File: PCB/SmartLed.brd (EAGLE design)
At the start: 82.5 x 70 mm, 46 parts, among them IC2 DS1307, IC3 MEGA8-P, K1 G5LE, Q1 32.768khz, T1 BC337

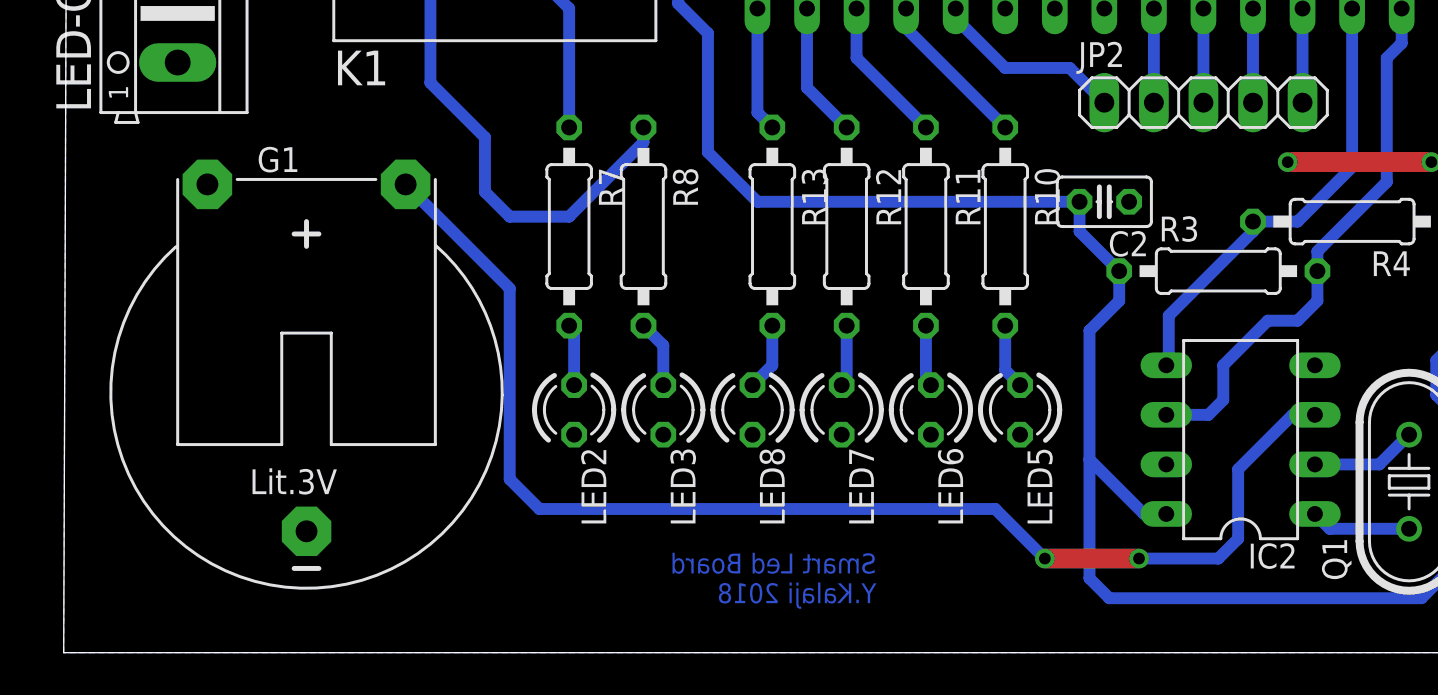
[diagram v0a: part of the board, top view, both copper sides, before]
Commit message: Add 100n capacitor beside 3.6v lithium battery & change the battery footprint
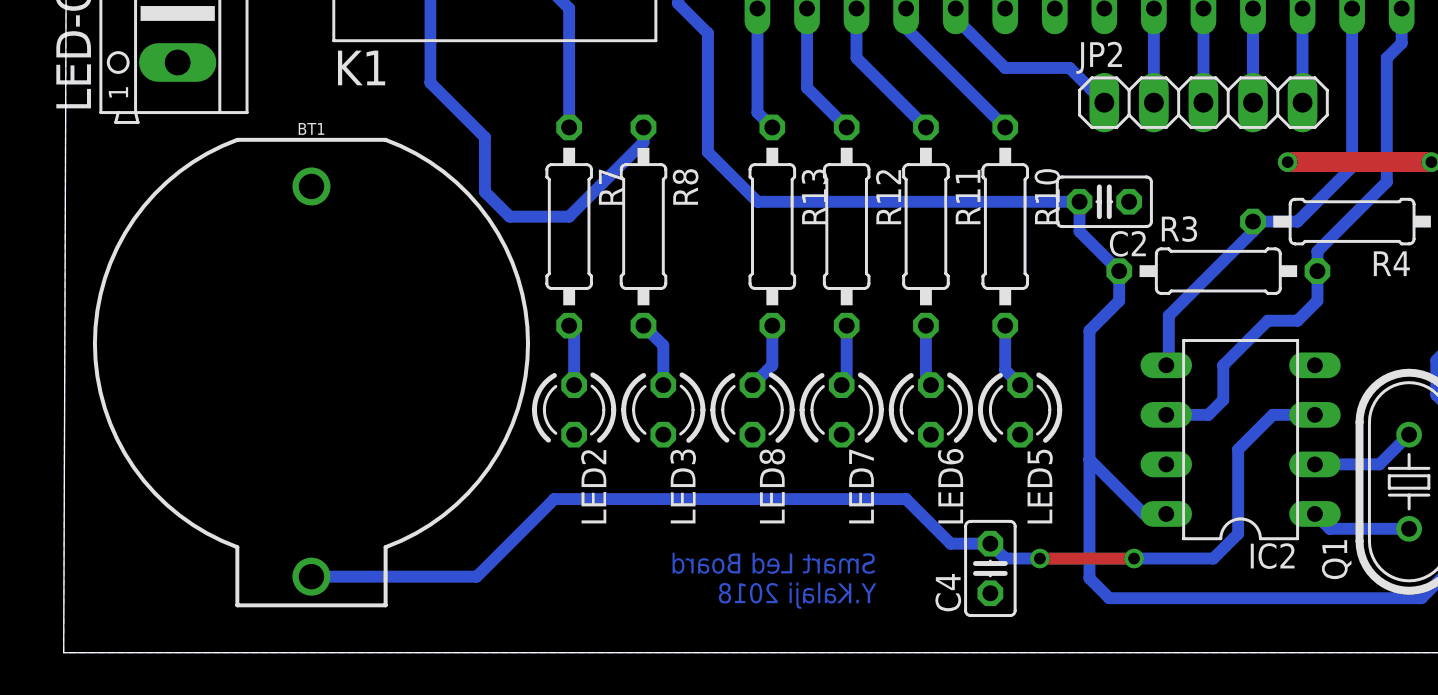
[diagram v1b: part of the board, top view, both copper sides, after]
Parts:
- removed G1: CR2032H, battery:CR2032H
- added BT1: (no value), SparkFun-Batteries:BATTCOM_20MM_PTH
- added C4: 100nf, rcl:C025-025X050
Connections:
- removed net N$18: G1.+, IC2.3
- new net N$44: BT1.1, C4.2, IC2.3
- net GND: now also BT1.2, C4.1; no longer G1.-
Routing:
- net N$18: track 65.4 -> 0.00 mm, vias 2 -> 0
- net N$44: track 0.00 -> 59.9 mm, vias 0 -> 2
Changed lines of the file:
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@@
 <layer number="112" name="tSilk" color="7" fill="1" visible="no" active="yes"/>
 <layer number="113" name="ReferenceLS" color="7" fill="1" visible="no" active="no"/>
+<layer number="114" name="Badge_Outline" color="7" fill="1" visible="yes" active="yes"/>
+<layer number="115" name="ReferenceISLANDS" color="7" fill="1" visible="yes" active="yes"/>
 <layer number="116" name="Patch_BOT" color="9" fill="4" visible="no" active="yes"/>
 <layer number="118" name="Rect_Pads" color="7" fill="1" visible="no" active="no"/>
@@
 <element name="C3" library="rcl" package="E2,5-5" value="4.7uf" x="56.642" y="88.9" rot="R270"/>
 <element name="D1" library="diode" package="DO35-7" value="1N4148DO35-7" x="22.098" y="86.36"/>
-<element name="G1" library="battery" package="CR2032H" value="CR2032H" x="8.636" y="42.926"/>
 <element name="IC2" library="adafruit" package="DIL08" value="DS1307" x="56.515" y="40.64" rot="R90"/>
 <element name="IC3" library="atmel" package="DIL28-3" value="MEGA8-P" x="48.26" y="66.548" rot="R180">
@@
 <element name="JP2" library="pinhead" package="1X05" value="" x="54.61" y="57.912"/>
 <element name="C1" library="rcl" package="E2,5-5" value="4.7uf" x="73.406" y="34.798" rot="R270"/>
+<element name="C4" library="rcl" package="C025-025X050" value="100nf" x="43.688" y="34.036" rot="R90"/>
+<element name="BT1" library="SparkFun-Batteries" package="BATTCOM_20MM_PTH" value="" x="8.89" y="45.466" rot="R270">
+<attribute name="SF_SKU" value="PRT-00783" x="8.89" y="45.466" size="1.778" layer="27" rot="R270" display="off"/>
+<attribute name="PROD_ID" value="BATT-09031" x="8.89" y="45.466" size="1.778" layer="27" rot="R270" display="off"/>
+</element>
 </elements>
 <signals>
@@
 <contactref element="OK1" pad="3"/>
 <contactref element="IC2" pad="4"/>
-<contactref element="G1" pad="-"/>
 <contactref element="IC3" pad="8"/>
 <contactref element="T1" pad="1"/>
@@
 <via x="73.152" y="58.42" extent="1-16" drill="0.6" shape="square"/>
 <contactref element="C1" pad="-"/>
+<contactref element="C4" pad="1"/>
+<contactref element="BT1" pad="2"/>
 </signal>
 <signal name="AVCC">
@@
 <wire x1="59.436" y1="51.816" x2="62.23" y2="54.61" width="0.6096" layer="16"/>
 </signal>
-<signal name="N$18">
-<contactref element="G1" pad="+"/>
-<contactref element="IC2" pad="3"/>
-<wire x1="43.942" y1="37.084" x2="20.574" y2="37.084" width="0.6096" layer="16"/>
-<wire x1="20.574" y1="37.084" x2="19.05" y2="38.608" width="0.6096" layer="16"/>
-<wire x1="19.05" y1="38.608" x2="19.05" y2="48.387" width="0.6096" layer="16"/>
-<wire x1="19.05" y1="48.387" x2="13.716" y2="53.721" width="0.6096" layer="16"/>
-<wire x1="60.325" y1="41.91" x2="59.182" y2="41.91" width="0.6096" layer="16"/>
-<wire x1="59.182" y1="41.91" x2="56.388" y2="39.116" width="0.6096" layer="16"/>
-<wire x1="56.388" y1="39.116" x2="56.388" y2="35.56" width="0.6096" layer="16"/>
-<wire x1="56.388" y1="35.56" x2="55.372" y2="34.544" width="0.6096" layer="16"/>
-<wire x1="55.372" y1="34.544" x2="51.308" y2="34.544" width="0.6096" layer="16"/>
-<via x="51.308" y="34.544" extent="1-16" drill="0.6" shape="square"/>
-<wire x1="51.308" y1="34.544" x2="46.482" y2="34.544" width="1.016" layer="1"/>
-<via x="46.482" y="34.544" extent="1-16" drill="0.6" shape="square"/>
-<wire x1="43.942" y1="37.084" x2="46.482" y2="34.544" width="0.6096" layer="16"/>
-</signal>
 <signal name="N$21">
 <contactref element="Q1" pad="1"/>
@@
 <wire x1="47.752" y1="59.69" x2="44.45" y2="59.69" width="0.6096" layer="16"/>
 </signal>
+<signal name="N$44">
+<contactref element="C4" pad="2"/>
+<contactref element="IC2" pad="3"/>
+<contactref element="BT1" pad="1"/>
+<wire x1="8.89" y1="33.616" x2="17.36" y2="33.616" width="0.6096" layer="16"/>
+<wire x1="17.36" y1="33.616" x2="21.336" y2="37.592" width="0.6096" layer="16"/>
+<wire x1="21.336" y1="37.592" x2="39.37" y2="37.592" width="0.6096" layer="16"/>
+<wire x1="39.37" y1="37.592" x2="41.656" y2="35.306" width="0.6096" layer="16"/>
+<wire x1="41.656" y1="35.306" x2="43.688" y2="35.306" width="0.6096" layer="16"/>
+<via x="46.228" y="34.544" extent="1-16" drill="0.6" shape="square"/>
+<wire x1="46.228" y1="34.544" x2="51.054" y2="34.544" width="0.6096" layer="1"/>
+<via x="51.054" y="34.544" extent="1-16" drill="0.6" shape="square"/>
+<wire x1="51.054" y1="34.544" x2="55.118" y2="34.544" width="0.6096" layer="16"/>
+<wire x1="55.118" y1="34.544" x2="56.388" y2="35.814" width="0.6096" layer="16"/>
+<wire x1="56.388" y1="35.814" x2="56.388" y2="40.132" width="0.6096" layer="16"/>
+<wire x1="56.388" y1="40.132" x2="58.166" y2="41.91" width="0.6096" layer="16"/>
+<wire x1="58.166" y1="41.91" x2="60.325" y2="41.91" width="0.6096" layer="16"/>
+<wire x1="43.688" y1="35.306" x2="44.45" y2="34.544" width="0.6096" layer="16"/>
+<wire x1="44.45" y1="34.544" x2="46.228" y2="34.544" width="0.6096" layer="16"/>
+</signal>
 </signals>

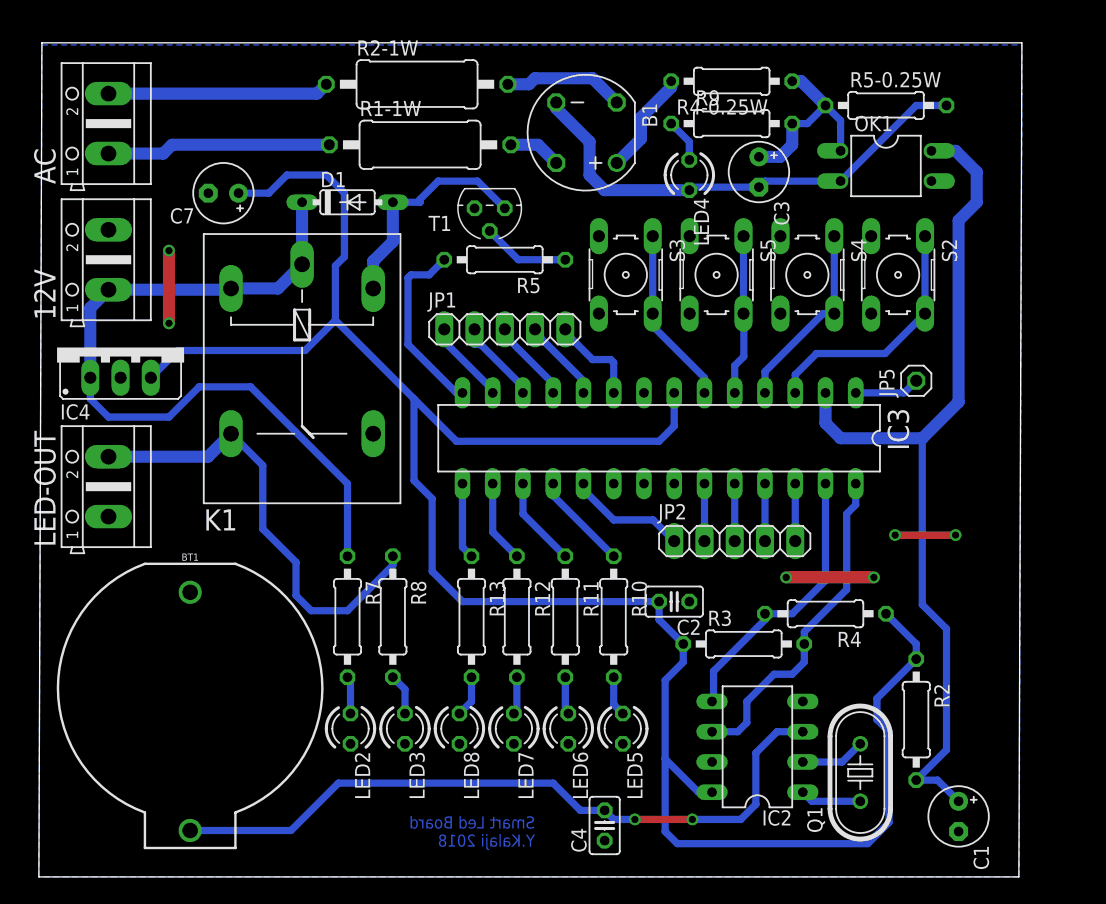
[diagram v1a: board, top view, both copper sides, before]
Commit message: Infrared receiver was added & crystal footprint size was corrected
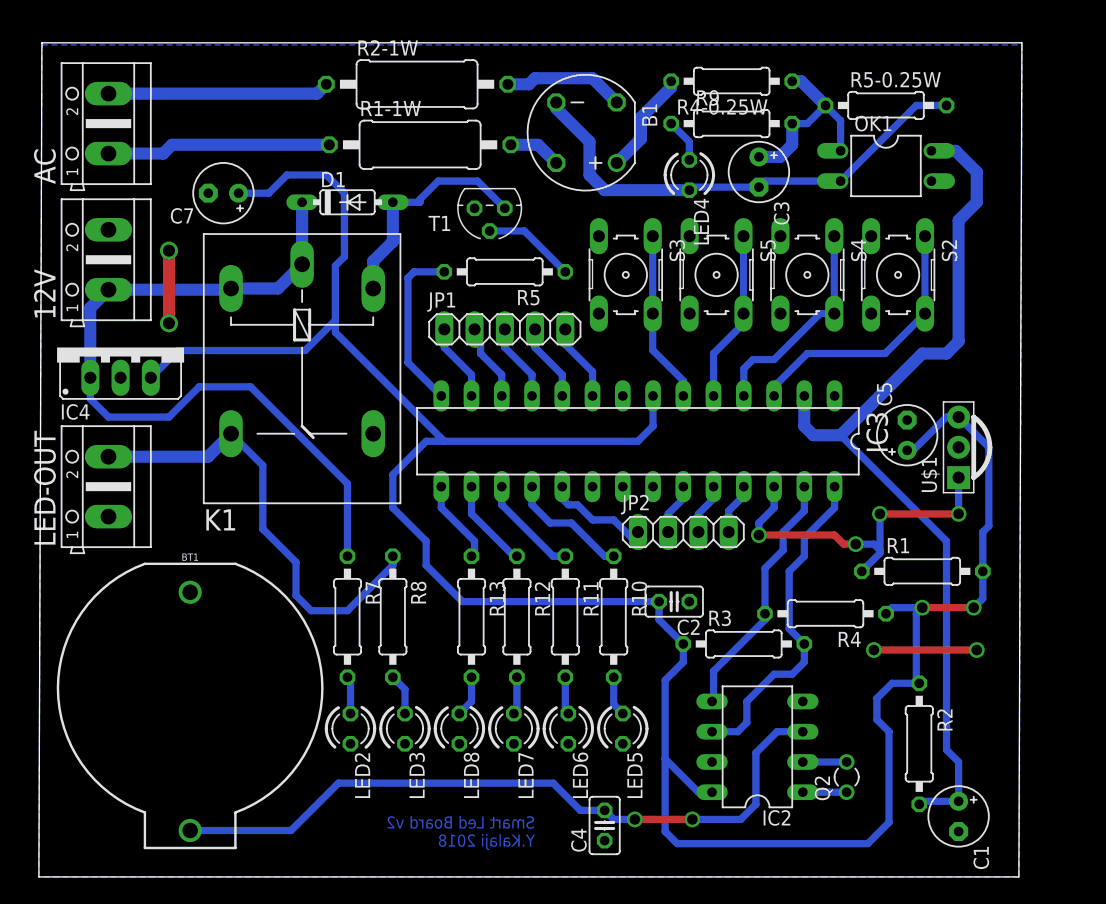
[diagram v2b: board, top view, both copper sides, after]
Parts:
- removed JP5: (no value), pinhead:1X01
- removed Q1: 32.768khz, crystal:HC49U70
- added C5: 4.7uf, rcl:E2,5-5
- added Q2: 32.768khz, crystal:TC26V
- added R1: 10k, rcl:0207/10
- added U$1: PNA460XM, adafruit:PNA460XM
- JP2: device pinhead:1X05 -> pinhead:1X04
- moved JP2 4.38 mm to (50.3, 58.7)
- moved R2 2.05 mm to (70.1, 40.9)
- moved IC3 1.80 mm to (46.5, 66.3)
- moved R5 1.02 mm to (35.3, 80.5)
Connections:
- removed net N$36: IC3.26, JP2.5
- removed net N$43: IC3.1, JP5.1
- new net N$46: IC3.26, R1.1, U$1.1
- net +5V: now also C5.+, R1.2, U$1.3
- net GND: now also C5.-, U$1.2
- net N$21: now also Q2.1; no longer Q1.1
- net N$22: now also Q2.2; no longer Q1.2
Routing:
- net N$46: track 0.00 -> 30.4 mm, vias 0 -> 4
- net +5V: track 176.0 -> 206.3 mm, vias 0 -> 2
- net N$43: track 5.50 -> 0.00 mm
- net N$36: track 4.83 -> 0.00 mm
- net GND: track 18.5 -> 14.7 mm, vias 6 -> 4
- net N$13: track 23.6 -> 21.2 mm
- net N$32: track 16.1 -> 18.3 mm
- net N$26: track 8.20 -> 10.2 mm
- net N$11: track 74.9 -> 76.7 mm
- net N$22: track 5.46 -> 3.68 mm
- net N$21: track 5.14 -> 3.68 mm
- net N$41: track 7.91 -> 6.53 mm
- net N$10: track 15.5 -> 14.3 mm
- net N$24: track 7.57 -> 8.65 mm
- net N$40: track 9.92 -> 8.94 mm
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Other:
- board text added: "Smart Led Board v2 Y.Kalaji 2018"
- board text removed: "Smart Led Board Y.Kalaji 2018"

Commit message: Refactor PCB design (several enhancements)
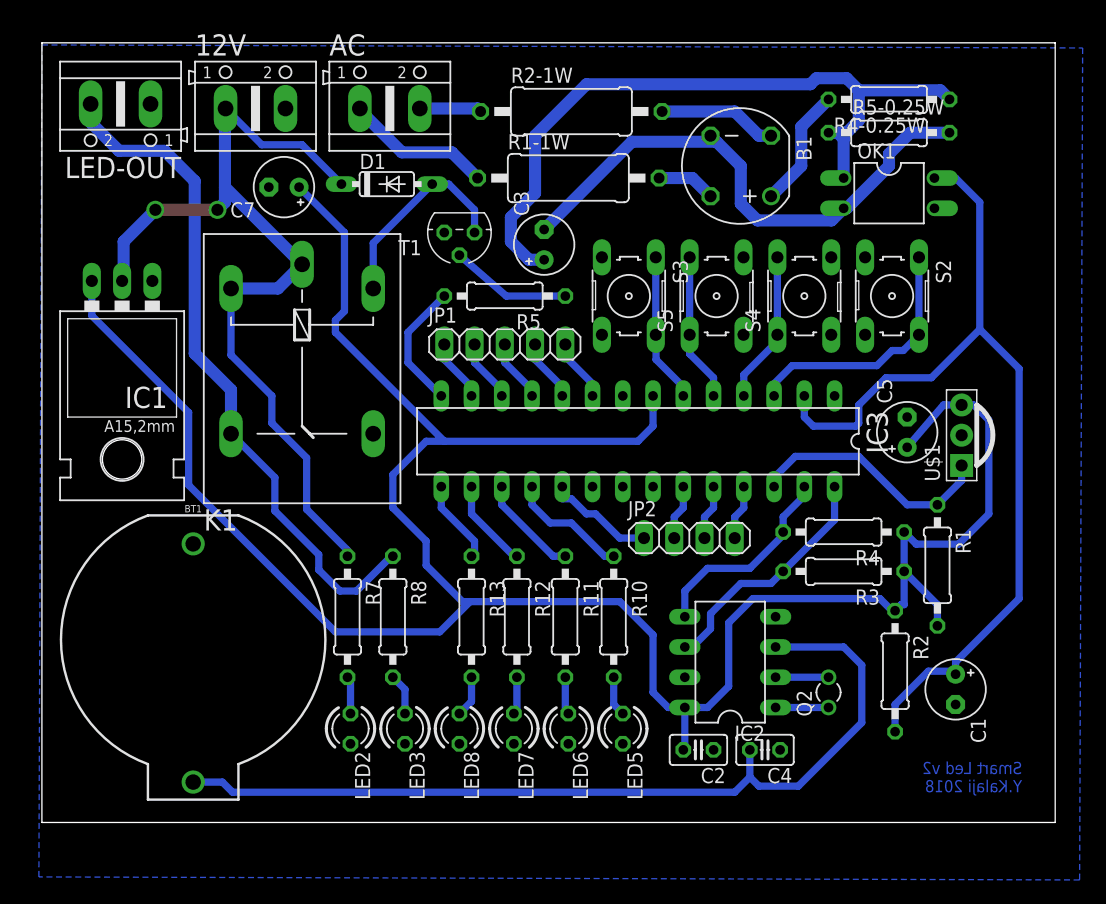
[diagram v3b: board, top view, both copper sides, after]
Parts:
- removed IC4: (no value), v-reg:78XXS
- removed LED4: (no value), led:LED3MM
- removed R9: 330, rcl:0207/10
- added IC1: (no value), v-reg:79XXL
- moved LED-OUT 32.1 mm to (3.05, 94.6), turned to 180 degrees
- moved AC 23.7 mm to (25.7, 94.2), turned to 0 degrees
- moved C3 19.0 mm to (38.6, 82.8), turned to 90 degrees
- moved 12V 17.7 mm to (14.4, 94.2), turned to 0 degrees
- moved C4 14.9 mm to (57.1, 40.4), turned to 180 degrees
- moved R4-0.25W 13.3 mm to (67.6, 95.0)
- moved B1 13.3 mm to (55.1, 89.4)
- moved R2-1W 13.2 mm to (40.9, 94.0)
- moved R1-1W 12.8 mm to (40.6, 88.4)
- moved C2 12.6 mm to (51.6, 40.4)
- moved C1 10.7 mm to (73.2, 45.5)
- moved R3 10.4 mm to (63.8, 55.4), turned to 180 degrees
- moved IC2 7.47 mm to (54.2, 47.8)
- moved Q2 7.27 mm to (62.5, 45.2)
- moved R4 7.03 mm to (63.8, 58.7)
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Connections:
- removed net N$19: LED4.A, R9.1
- net +12V: now also IC1.IN; no longer IC4.IN
- net +5V: now also IC1.OUT; no longer IC4.OUT
- net GND: now also IC1.GND; no longer IC4.GND
- net N$6: no longer R9.2
- net N$7: no longer LED4.K
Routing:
- net N$6: track 16.4 -> 60.2 mm
- net N$8: track 37.9 -> 57.5 mm
- net GND: track 14.7 -> 0.00 mm, vias 4 -> 0
- net N$44: track 59.9 -> 74.5 mm, vias 2 -> 0
- net N$2: track 18.6 -> 5.21 mm
- net +12V: track 64.9 -> 76.5 mm, vias 0 -> 2
- net N$46: track 30.4 -> 21.0 mm, vias 4 -> 0
- net N$12: track 28.0 -> 20.5 mm
- net N$1: track 18.8 -> 12.4 mm
- net N$7: track 40.7 -> 45.3 mm
- net N$32: track 18.3 -> 13.8 mm
- net N$13: track 21.2 -> 17.2 mm
- net N$19: track 3.68 -> 0.00 mm
- net N$10: track 14.3 -> 10.8 mm
- net N$9: track 7.77 -> 10.2 mm
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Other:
- board size 82.5 x 70 mm -> 85.1 x 65.5 mm
- board text added: "Smart Led v2 Y.Kalaji 2018"
- board text removed: "Smart Led Board v2 Y.Kalaji 2018"

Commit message: Add PIR sensor pins to PCB
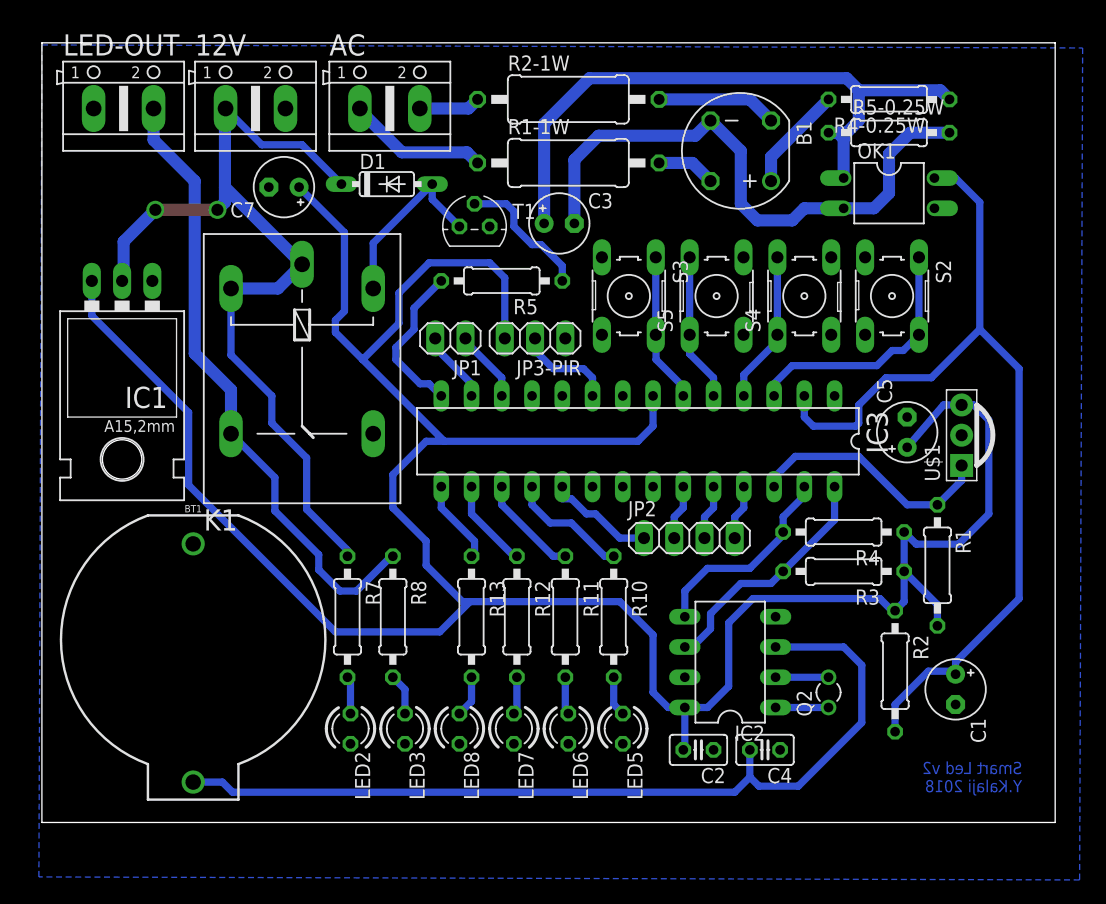
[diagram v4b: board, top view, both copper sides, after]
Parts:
- added JP3-PIR: (no value), pinhead:1X03
- JP1: device pinhead:1X05 -> pinhead:1X02
- moved JP1 4.60 mm to (30.7, 74.9), turned to 180 degrees
- moved C3 2.18 mm to (39.9, 84.6), turned to 0 degrees
- moved T1 1.37 mm to (32.8, 84.3), turned to 0 degrees
- moved R5 1.30 mm to (35.1, 79.8)
- moved R1-1W 1.27 mm to (40.6, 89.7)
- moved B1 1.27 mm to (55.1, 90.7)
- moved R2-1W 1.05 mm to (40.6, 95.0)
- moved LED-OUT 0.46 mm to (3.30, 94.2), turned to 0 degrees
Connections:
- removed net N$35: IC3.11, JP1.3
- removed net N$41: IC3.9, JP1.5
- removed net N$42: IC3.10, JP1.4
- new net N$19: IC3.9, JP3-PIR.2
- net +5V: now also JP3-PIR.3
- net GND: now also JP3-PIR.1
- net N$37: now also JP1.1; no longer JP1.2
- net N$39: now also JP1.2; no longer JP1.1
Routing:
- net +5V: track 208.5 -> 230.8 mm
- net N$19: track 0.00 -> 8.31 mm
- net N$6: track 60.2 -> 54.3 mm
- net N$42: track 5.26 -> 0.00 mm
- net N$35: track 5.26 -> 0.00 mm
- net N$41: track 5.26 -> 0.00 mm
- net N$8: track 57.5 -> 52.6 mm
- net N$7: track 45.3 -> 49.3 mm
- net N$10: track 10.8 -> 13.3 mm
- net N$14: track 17.2 -> 15.3 mm
- net N$9: track 10.2 -> 11.5 mm
- net N$5: track 10.1 -> 8.86 mm
- net N$39: track 5.26 -> 6.09 mm
- net N$37: track 5.26 -> 6.09 mm
- net N$1: track 12.4 -> 11.9 mm
